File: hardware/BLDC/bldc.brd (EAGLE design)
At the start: 51.1 x 40 mm, 83 parts, among them J1 PWR_2_XT30PW-M, J2 LINEAR_35040500391, J3 LINEAR_85040500891, U1 MA702, U10 MCP2542FD, U11 LDFM33PUR, U2 DRV8323RS, U3 TPN7R006PL, U4 TPN7R006PL, U5 TPN7R006PL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

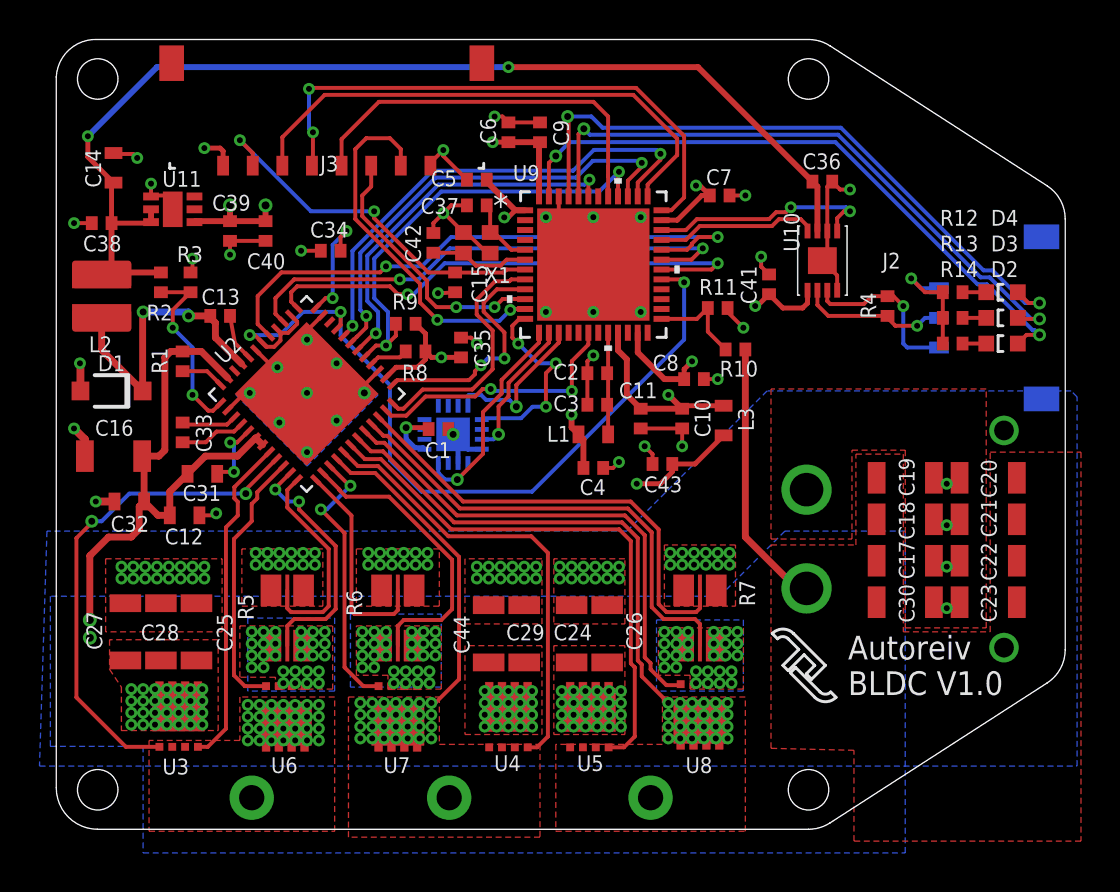
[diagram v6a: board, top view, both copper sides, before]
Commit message: No more via-in-pad
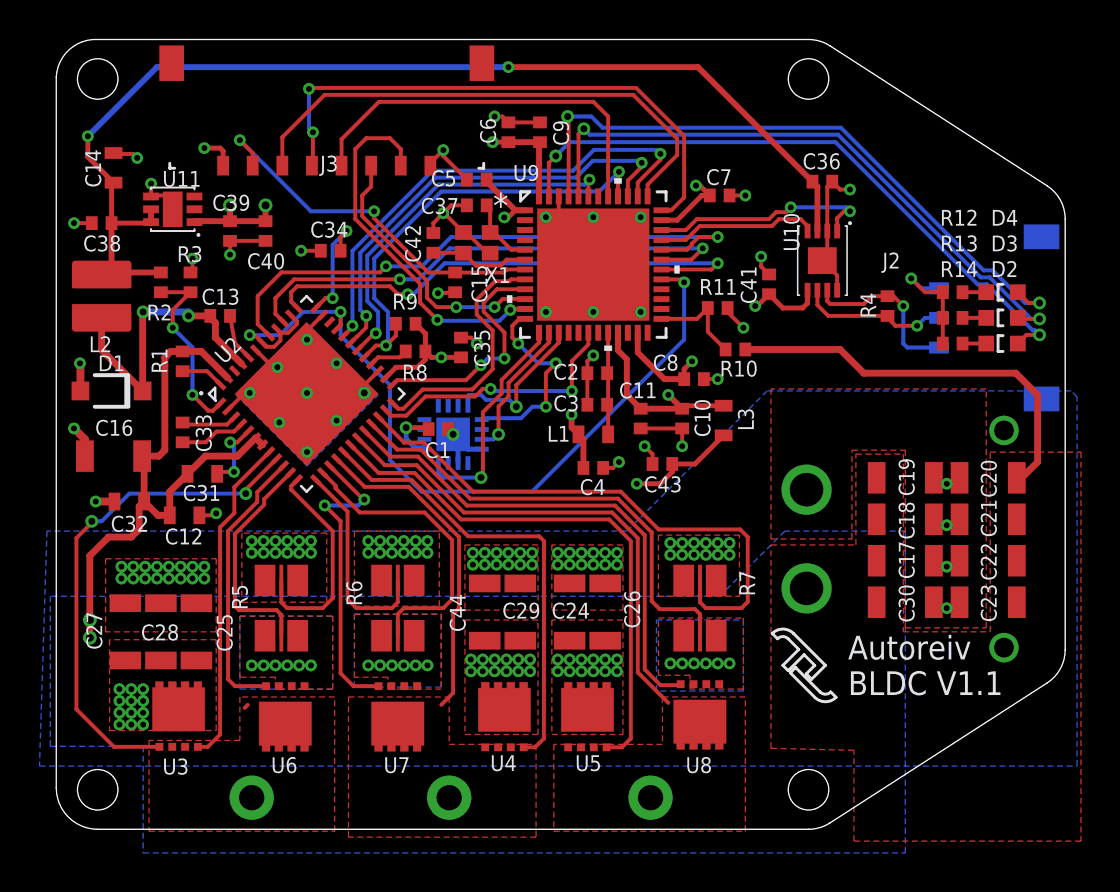
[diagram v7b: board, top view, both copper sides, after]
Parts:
- moved C29 1.12 mm to (23.4, 11.0)
- moved C44 1.12 mm to (21.6, 11.0)
- moved C24 1.10 mm to (25.9, 11.0)
- moved C26 1.10 mm to (27.7, 11.0)
- moved R5 0.58 mm to (11.3, 11.2)
- moved R6 0.50 mm to (17.2, 11.2)
- moved R7 0.50 mm to (32.5, 11.2)
- moved U4 0.20 mm to (22.6, 5.70)
- moved U5 0.10 mm to (26.8, 5.70)
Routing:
- net +24V: track 42.3 -> 50.2 mm, vias 74 -> 38
- net SNC: track 23.6 -> 28.3 mm
- net GLB: track 14.1 -> 15.6 mm
- net SPA: track 12.6 -> 11.5 mm, vias 2 -> 0
- net ENC_SCK: track 10.7 -> 11.3 mm
- net GLA: track 13.5 -> 14.0 mm
- net SHB: track 16.4 -> 16.7 mm, vias 28 -> 0
- net SHA: track 25.5 -> 25.8 mm, vias 30 -> 2
- net SHC: vias 24 -> 0
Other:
- board text added: "Autoreiv BLDC V1.1"
- board text removed: "Autoreiv BLDC V1.0"
